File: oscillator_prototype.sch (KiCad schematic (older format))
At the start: 94 parts, among them J1 PJ398SM, J10 Conn_01x06_Male, J11 Conn_01x06_Female, J12 Conn_01x06_Male, J13 Conn_01x06_Female, J14 Conn_01x06_Male, J3 PJ398SM, J4 PJ398SM, J6 PJ398SM, J7 Eurorack power, J8 PJ398SM, J9 Conn_01x06_Female, Q1 MMBT3904, Q2 MMBT3906, Q3 BC857BS, Q4 MMBT3904, Q5 MMBT3904, SW1 Sync Mode, U1 LT1013-SOIC, U10 LM4040AIM3-5, U11 LM4040AIM3-5, U2 TL074, U3 LM13700, U4 LM311, U5 LM4040AIM3-2.5, U6 DG418, U7 LM311, U8 LM4040AIM3-2.5, U9 LM4040AIM3-2.5

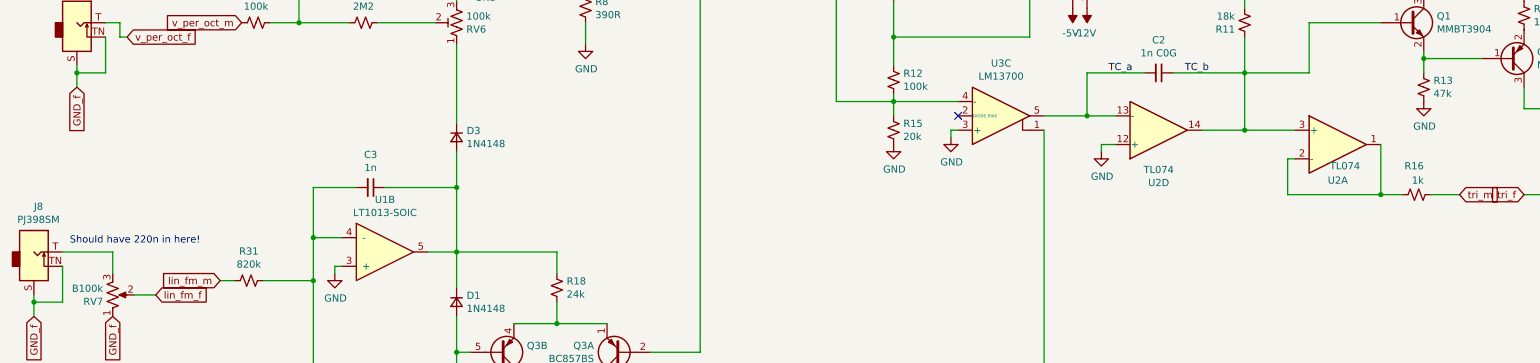
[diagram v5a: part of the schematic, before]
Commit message: Correct -12v connection in saw shaper; add missing AC couple cap to linear FM input
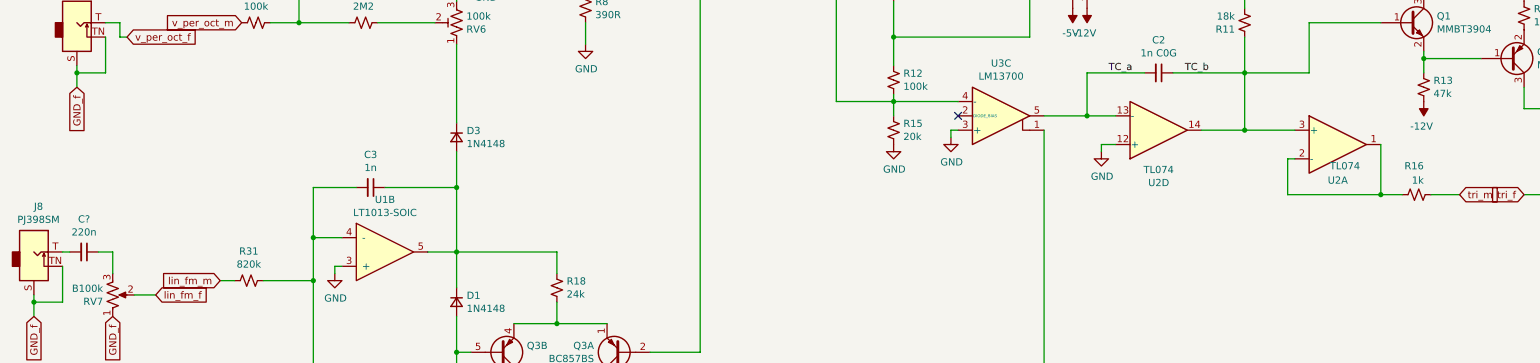
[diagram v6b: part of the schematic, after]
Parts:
- added C?: 220n, Capacitor_SMD:C_0805_2012Metric_Pad1.18x1.45mm_HandSolder, symbol Device:C_Small
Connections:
- net -12V: now also R13.1
- net GND: no longer R13.1
- net at RV7.3: now also C?.1; no longer J8.T
- new net: C?.2, J8.T
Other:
- note removed: "Should have 220n in here!"
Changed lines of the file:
@@
 $EndComp
 Connection ~ 10100 4000
-$Comp
-L power:GND #PWR019
-U 1 1 5FCFD842
-P 10400 3350
-F 0 "#PWR019" H 10400 3100 50  0001 C CNN
-F 1 "GND" H 10405 3177 50  0000 C CNN
-F 2 "" H 10400 3350 50  0001 C CNN
-F 3 "" H 10400 3350 50  0001 C CNN
-	1    10400 3350
-	1    0    0    -1
-$EndComp
 Wire Wire Line
 	10400 3150 10400 3050
@@
 Wire Wire Line
 	1300 2800 1200 2800
-Wire Wire Line
-	1250 4400 900  4400
 Text GLabel 1550 4700 2    50   Input ~ 0
 lin_fm_f
@@
 $EndComp
 Connection ~ 4550 1900
-Text Notes 950  4350 0    50   ~ 0
-Should have 220n in here!
 $Comp
 L Device:R_Small_US R11
@@
 	-1   0    0    1
 $EndComp
+$Comp
+L power:-12V #PWR?
+U 1 1 5FFF22B1
+P 10400 3350
+F 0 "#PWR?" H 10400 3450 50  0001 C CNN
+F 1 "-12V" H 10415 3523 50  0000 C CNN
+F 2 "" H 10400 3350 50  0001 C CNN
+F 3 "" H 10400 3350 50  0001 C CNN
+	1    10400 3350
+	-1   0    0    1
+$EndComp
+$Comp
+L Device:C_Small C?
+U 1 1 600B4DC7
+P 1050 4400
+F 0 "C?" V 821 4400 50  0000 C CNN
+F 1 "220n" V 912 4400 50  0000 C CNN
+F 2 "Capacitor_SMD:C_0805_2012Metric_Pad1.18x1.45mm_HandSolder" H 1050 4400 50  0001 C CNN
+F 3 "~" H 1050 4400 50  0001 C CNN
+	1    1050 4400
+	0    1    1    0
+$EndComp
+Wire Wire Line
+	950  4400 900  4400
+Wire Wire Line
+	1150 4400 1250 4400
 $EndSCHEMATC
